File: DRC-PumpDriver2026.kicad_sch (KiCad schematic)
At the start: 28 parts, among them J1 STLINK, J10 VIN_PWR, J2 CAN, J3 CAN, J4 PUMP1, J5 PUMP2, J6 PUMP3, J7 PUMP4, J8 PUMP5, J9 PUMP6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

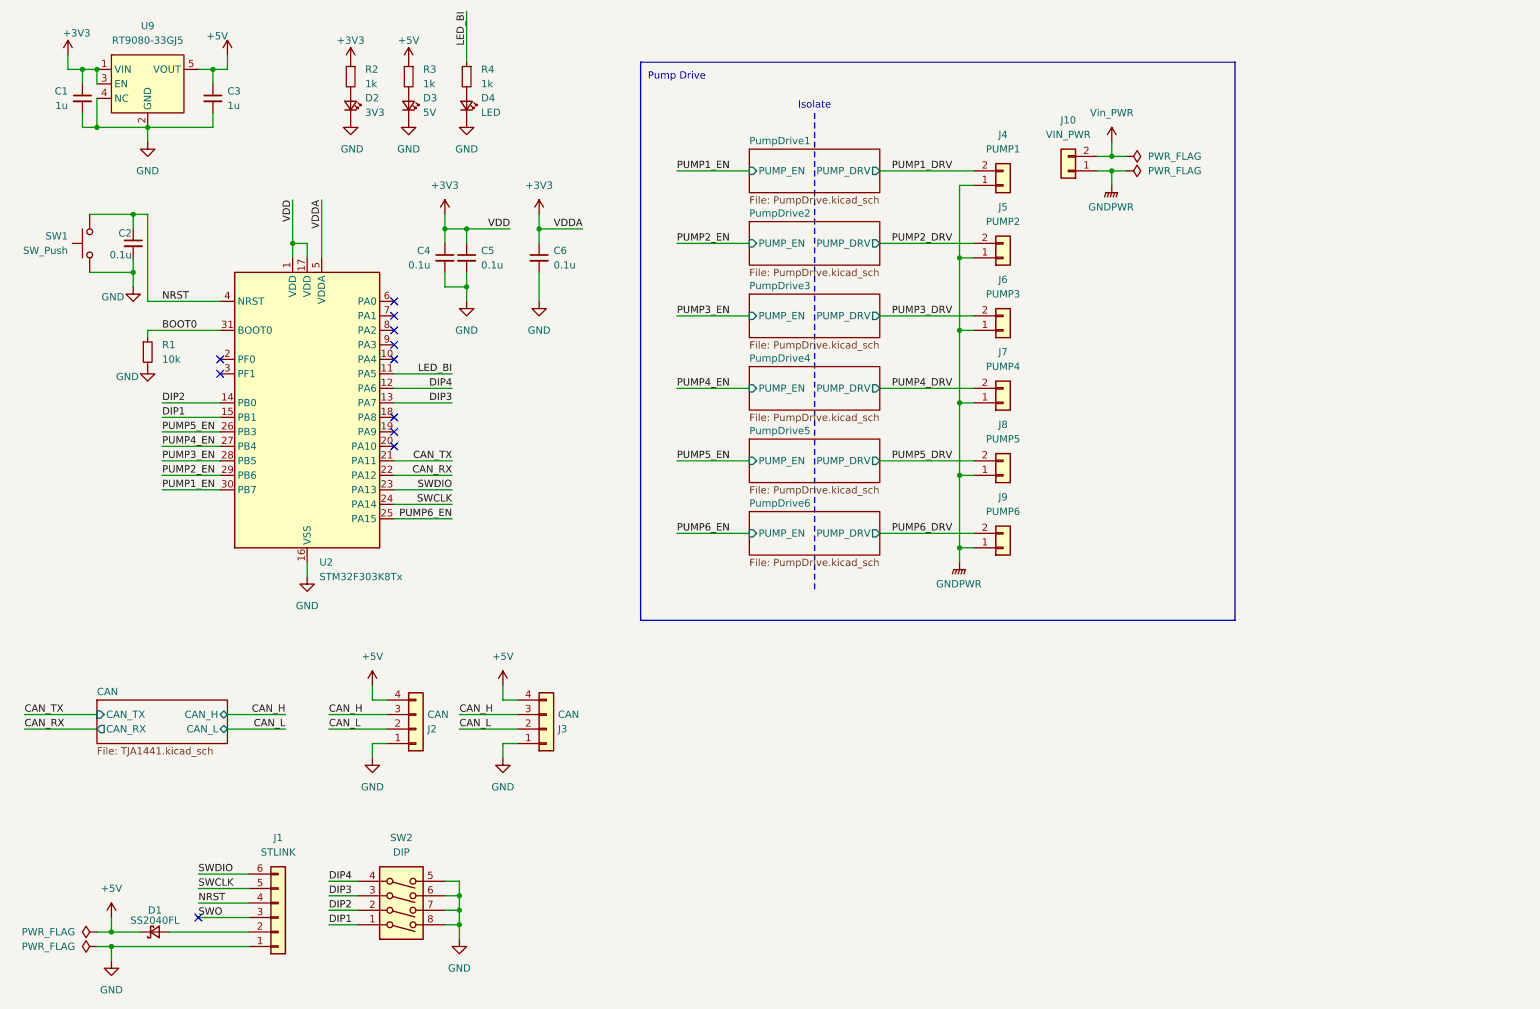
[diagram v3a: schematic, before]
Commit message: STLINK書込みをボックスヘッダへ、USB追加、v0.1.0
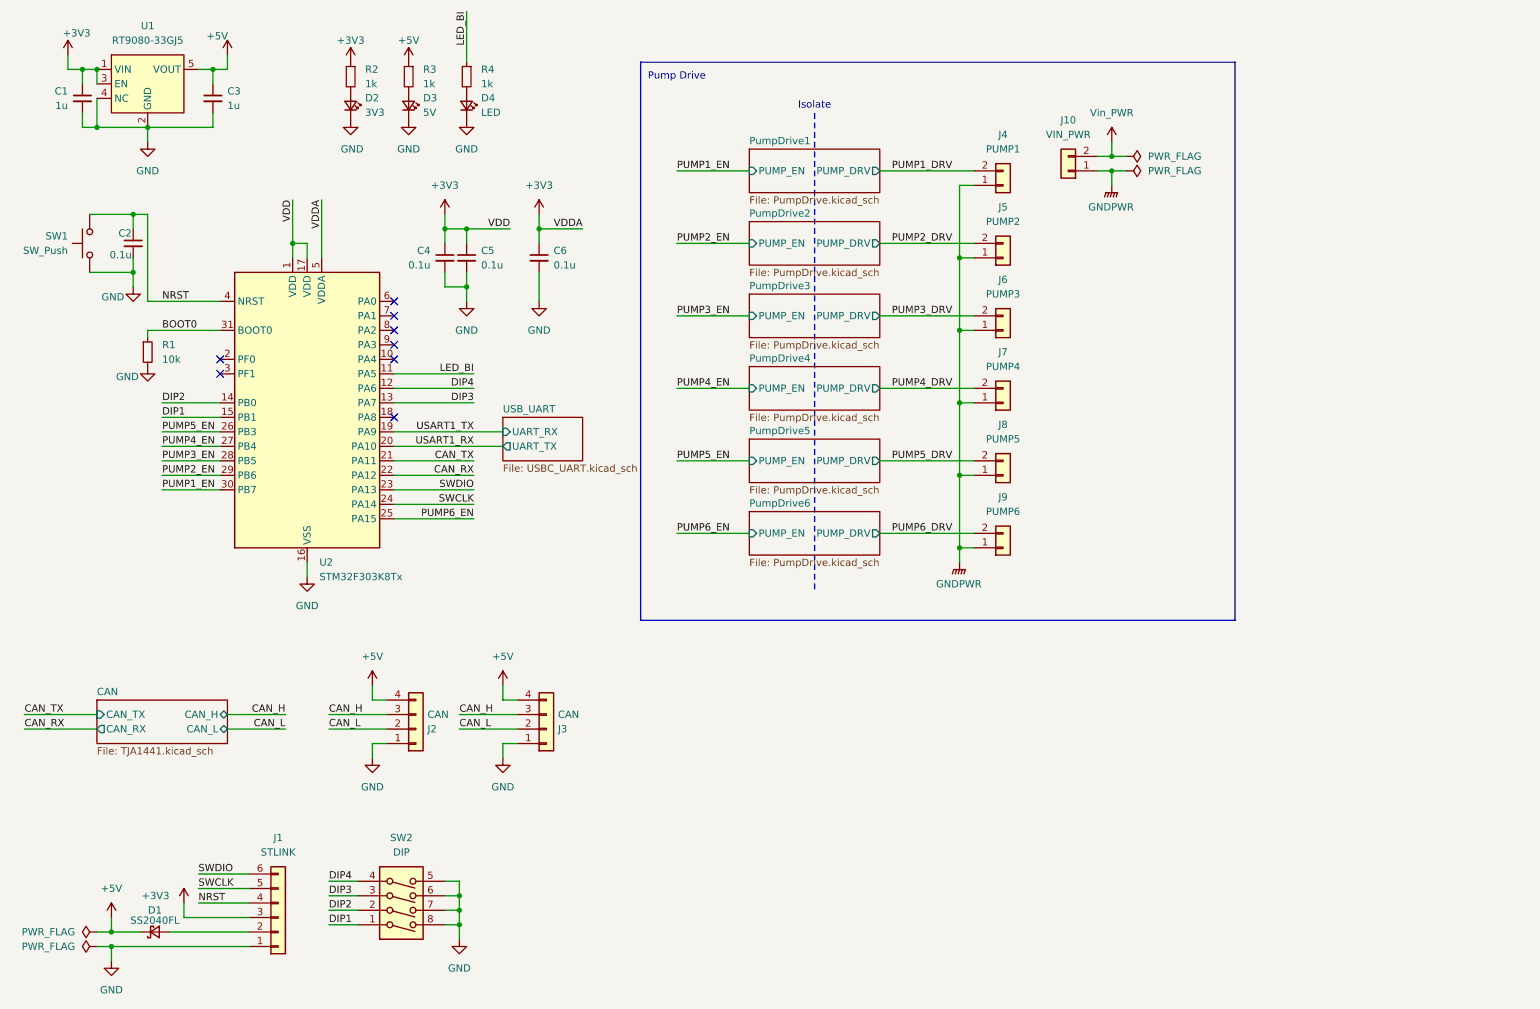
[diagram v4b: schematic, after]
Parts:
- J1: footprint Connector_JST:JST_PH_S6B-PH-K_1x06_P2.00mm_Horizontal -> Connector_IDC:IDC-Header_2x03_P2.54mm_Vertical
- renumbered U9 to U1
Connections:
- net SWO is gone; now on net +3V3: J1.3 (Pin_3)
- net USART1_TX: now reaches U2.19 (PA9)
- net USART1_RX: now reaches U2.20 (PA10)
- no-connect marks 11 -> 8
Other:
- added sheet USB_UART (USBC_UART.kicad_sch)
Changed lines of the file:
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@@
 	)
 	(no_connect
-		(at 85.09 87.63)
-	)
-	(no_connect
 		(at 85.09 67.31)
 	)
@@
 	)
 	(no_connect
-		(at 85.09 90.17)
-	)
-	(no_connect
-		(at 50.8 172.72)
-	)
-	(no_connect
 		(at 85.09 74.93)
 	)
@@
 	(wire
 		(pts
+			(xy 85.09 87.63) (xy 104.14 87.63)
+		)
+		(stroke
+			(width 0)
+			(type default)
+		)
+	)
+	(wire
+		(pts
 			(xy 41.91 64.77) (xy 54.61 64.77)
 		)
@@
 	(wire
 		(pts
+			(xy 48.26 170.18) (xy 48.26 172.72)
+		)
+		(stroke
+			(width 0)
+			(type default)
+		)
+	)
+	(wire
+		(pts
 			(xy 50.8 167.64) (xy 59.69 167.64)
 		)
@@
 	(wire
 		(pts
-			(xy 85.09 92.71) (xy 95.25 92.71)
+			(xy 85.09 92.71) (xy 99.06 92.71)
 		)
 		(stroke
@@
 	(wire
 		(pts
-			(xy 85.09 82.55) (xy 95.25 82.55)
+			(xy 85.09 82.55) (xy 99.06 82.55)
 		)
 		(stroke
@@
 	(wire
 		(pts
-			(xy 85.09 102.87) (xy 95.25 102.87)
+			(xy 85.09 102.87) (xy 99.06 102.87)
 		)
 		(stroke
@@
 	(wire
 		(pts
-			(xy 85.09 80.01) (xy 95.25 80.01)
+			(xy 85.09 80.01) (xy 99.06 80.01)
 		)
 		(stroke
@@
 	(wire
 		(pts
-			(xy 85.09 100.33) (xy 95.25 100.33)
+			(xy 85.09 100.33) (xy 99.06 100.33)
 		)
 		(stroke
@@
 	(wire
 		(pts
+			(xy 85.09 90.17) (xy 104.14 90.17)
+		)
+		(stroke
+			(width 0)
+			(type default)
+		)
+	)
+	(wire
+		(pts
 			(xy 72.39 46.99) (xy 72.39 57.15)
 		)
@@
 	(wire
 		(pts
+			(xy 48.26 172.72) (xy 59.69 172.72)
+		)
+		(stroke
+			(width 0)
+			(type default)
+		)
+	)
+	(wire
+		(pts
 			(xy 96.52 171.45) (xy 96.52 173.99)
 		)
@@
 	(wire
 		(pts
-			(xy 50.8 172.72) (xy 59.69 172.72)
-		)
-		(stroke
-			(width 0)
-			(type default)
-		)
-	)
-	(wire
-		(pts
 			(xy 30.48 31.75) (xy 30.48 34.29)
 		)
@@
 	(wire
 		(pts
-			(xy 85.09 97.79) (xy 95.25 97.79)
+			(xy 85.09 97.79) (xy 99.06 97.79)
 		)
 		(stroke
@@
 	(wire
 		(pts
-			(xy 85.09 95.25) (xy 95.25 95.25)
+			(xy 85.09 95.25) (xy 99.06 95.25)
 		)
 		(stroke
@@
 	(wire
 		(pts
-			(xy 85.09 77.47) (xy 95.25 77.47)
+			(xy 85.09 77.47) (xy 99.06 77.47)
 		)
 		(stroke
@@
 	)
 	(label "LED_BI"
-		(at 95.25 77.47 180)
+		(at 99.06 77.47 180)
 		(effects
 			(font
@@
 	)
 	(label "SWCLK"
-		(at 95.25 100.33 180)
+		(at 99.06 100.33 180)
 		(effects
 			(font
@@
 	)
 	(label "DIP3"
-		(at 95.25 82.55 180)
+		(at 99.06 82.55 180)
 		(effects
 			(font
@@
 	)
 	(label "PUMP6_EN"
-		(at 95.25 102.87 180)
+		(at 99.06 102.87 180)
 		(effects
 			(font
@@
 	)
 	(label "CAN_TX"
-		(at 95.25 92.71 180)
+		(at 99.06 92.71 180)
 		(effects
 			(font
@@
 		)
 	)
+	(label "USART1_TX"
+		(at 99.06 87.63 180)
+		(effects
+			(font
+				(size 1.27 1.27)
+			)
+			(justify right bottom)
+		)
+	)
 	(label "PUMP1_DRV"
 		(at 182.88 41.91 180)
@@
 	)
 	(label "SWDIO"
-		(at 95.25 97.79 180)
+		(at 99.06 97.79 180)
 		(effects
 			(font
@@
 		)
 	)
-	(label "CAN_L"
-		(at 66.04 139.7 180)
+	(label "USART1_RX"
+		(at 99.06 90.17 180)
 		(effects
 			(font
@@
 		)
 	)
-	(label "SWO"
-		(at 50.8 172.72 0)
+	(label "CAN_L"
+		(at 66.04 139.7 180)
 		(effects
 			(font
 				(size 1.27 1.27)
 			)
-			(justify left bottom)
+			(justify right bottom)
 		)
 	)
@@
 	)
 	(label "CAN_RX"
-		(at 95.25 95.25 180)
+		(at 99.06 95.25 180)
 		(effects
 			(font
@@
 	)
 	(label "DIP4"
-		(at 95.25 80.01 180)
+		(at 99.06 80.01 180)
 		(effects
 			(font
@@
 		(dnp no)
 		(fields_autoplaced yes)
-		(property "Reference" "#PWR02"
+		(property "Reference" "#PWR03"
 			(at 35.56 186.69 0)
 			(effects
@@
 			(project "DRC-PumpDriver2026"
 				(path "/cf42be67-fab3-494c-b2b5-38aff4068810"
-					(reference "#PWR02")
+					(reference "#PWR03")
 					(unit 1)
 				)
@@
 		(on_board yes)
 		(dnp no)
-		(property "Reference" "#PWR07"
+		(property "Reference" "#PWR01"
 			(at 27.94 25.4 0)
 			(effects
@@
 			(project "DRC-PumpDriver2026"
 				(path "/cf42be67-fab3-494c-b2b5-38aff4068810"
-					(reference "#PWR07")
+					(reference "#PWR01")
 					(unit 1)
 				)
@@
 			)
 		)
-		(property "Footprint" "Connector_JST:JST_PH_S6B-PH-K_1x06_P2.00mm_Horizontal"
+		(property "Footprint" "Connector_IDC:IDC-Header_2x03_P2.54mm_Vertical"
 			(at 64.77 172.72 0)
 			(effects
@@
 		(on_board yes)
 		(dnp no)
-		(property "Reference" "#PWR03"
+		(property "Reference" "#PWR07"
 			(at 55.88 25.4 0)
 			(effects
@@
 			(project "DRC-PumpDriver2026"
 				(path "/cf42be67-fab3-494c-b2b5-38aff4068810"
-					(reference "#PWR03")
+					(reference "#PWR07")
 					(unit 1)
 				)
@@
 		(on_board yes)
 		(dnp no)
-		(property "Reference" "#PWR05"
+		(property "Reference" "#PWR06"
 			(at 41.91 82.55 0)
 			(effects
@@
 			(project "DRC-PumpDriver2026"
 				(path "/cf42be67-fab3-494c-b2b5-38aff4068810"
-					(reference "#PWR05")
+					(reference "#PWR06")
 					(unit 1)
 				)
@@
 		(dnp no)
 		(fields_autoplaced yes)
-		(property "Reference" "#PWR01"
+		(property "Reference" "#PWR02"
 			(at 35.56 176.53 0)
 			(effects
@@
 			(project "DRC-PumpDriver2026"
 				(path "/cf42be67-fab3-494c-b2b5-38aff4068810"
-					(reference "#PWR01")
+					(reference "#PWR02")
 					(unit 1)
 				)
@@
 	)
 	(symbol
+		(lib_id "power:+3V3")
+		(at 48.26 170.18 0)
+		(unit 1)
+		(exclude_from_sim no)
+		(in_bom yes)
+		(on_board yes)
+		(dnp no)
+		(fields_autoplaced yes)
+		(property "Reference" "#PWR050"
+			(at 48.26 173.99 0)
+			(effects
+				(font
+					(size 1.27 1.27)
+				)
+				(hide yes)
+			)
+		)
+		(property "Value" "+3V3"
+			(at 45.72 168.9099 0)
+			(effects
+				(font
+					(size 1.27 1.27)
+				)
+				(justify right)
+			)
+		)
+		(property "Footprint" ""
+			(at 48.26 170.18 0)
+			(effects
+				(font
+					(size 1.27 1.27)
+				)
+				(hide yes)
+			)
+		)
+		(property "Datasheet" ""
+			(at 48.26 170.18 0)
+			(effects
+				(font
+					(size 1.27 1.27)
+				)
+				(hide yes)
+			)
+		)
+		(property "Description" "Power symbol creates a global label with name \"+3V3\""
+			(at 48.26 170.18 0)
+			(effects
+				(font
+					(size 1.27 1.27)
+				)
+				(hide yes)
+			)
+		)
+		(pin "1"
+		)
+		(instances
+			(project "DRC-PumpDriver2026"
+				(path "/cf42be67-fab3-494c-b2b5-38aff4068810"
+					(reference "#PWR050")
+					(unit 1)
+				)
+			)
+		)
+	)
+	(symbol
 		(lib_id "MCU_ST_STM32F3:STM32F303K8Tx")
 		(at 69.85 85.09 0)
@@
 		(dnp no)
 		(fields_autoplaced yes)
-		(property "Reference" "U9"
+		(property "Reference" "U1"
 			(at 41.91 16.51 0)
 			(effects
@@
 			(project "DRC-PumpDriver2026"
 				(path "/cf42be67-fab3-494c-b2b5-38aff4068810"
-					(reference "U9")
+					(reference "U1")
 					(unit 1)
 				)
@@
 		(dnp no)
 		(fields_autoplaced yes)
-		(property "Reference" "#PWR06"
+		(property "Reference" "#PWR05"
 			(at 41.91 43.18 0)
 			(effects
@@
 			(project "DRC-PumpDriver2026"
 				(path "/cf42be67-fab3-494c-b2b5-38aff4068810"
-					(reference "#PWR06")
+					(reference "#PWR05")
 					(unit 1)
 				)
@@
 				)
 			)
+		)
+	)
+	(sheet
+		(at 104.14 85.09)
+		(size 13.97 7.62)
+		(exclude_from_sim no)
+		(in_bom yes)
+		(on_board yes)
+		(dnp no)
+		(fields_autoplaced yes)
+		(stroke
+			(width 0.1524)
+			(type solid)
+		)
+		(fill
+			(color 0 0 0 0.0000)
+		)
+		(property "Sheetname" "USB_UART"
+			(at 104.14 84.3784 0)
+			(effects
+				(font
+					(size 1.27 1.27)
+				)
+				(justify left bottom)
+			)
+		)
+		(property "Sheetfile" "USBC_UART.kicad_sch"
+			(at 104.14 93.2946 0)
+			(effects
+				(font
+					(size 1.27 1.27)
+				)
+				(justify left top)
+			)
+		)
+		(pin "UART_RX" input
+			(at 104.14 87.63 180)
+			(effects
+				(font
+					(size 1.27 1.27)
+				)
+				(justify left)
+			)
+		)
+		(pin "UART_TX" output
+			(at 104.14 90.17 180)
+			(effects
+				(font
+					(size 1.27 1.27)
+				)
+				(justify left)
+			)
+		)
+		(instances
+			(project "DRC-PumpDriver2026"
+				(path "/cf42be67-fab3-494c-b2b5-38aff4068810"
+					(page "9")
+				)
+			)

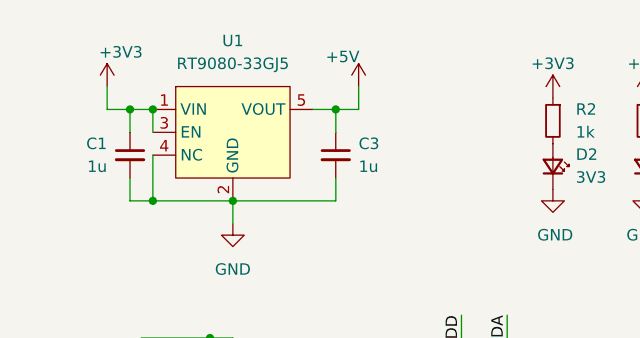
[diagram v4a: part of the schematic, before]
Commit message: レギュレータのフットプリントを修正
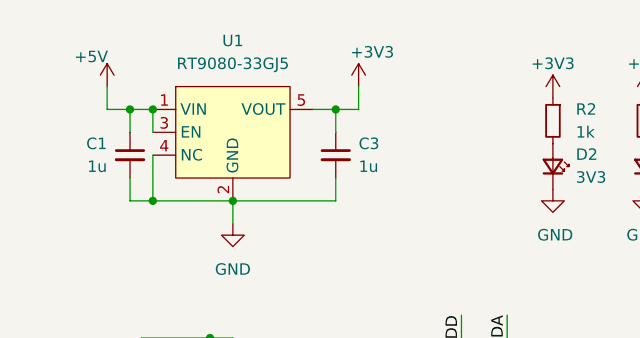
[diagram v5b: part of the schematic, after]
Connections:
- net +3V3: now also C3.1, U1.5 (VOUT); no longer C1.1, U1.1 (VIN), U1.3 (EN)
- net +5V: now also C1.1, U1.1 (VIN), U1.3 (EN); no longer C3.1, U1.5 (VOUT)
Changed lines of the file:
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@@
 	(symbol
 		(lib_id "power:+3V3")
-		(at 27.94 21.59 0)
+		(at 55.88 21.59 0)
 		(unit 1)
 		(exclude_from_sim no)
@@
 		(dnp no)
 		(property "Reference" "#PWR01"
-			(at 27.94 25.4 0)
+			(at 55.88 25.4 0)
 			(effects
 				(font
@@
 		)
 		(property "Value" "+3V3"
-			(at 29.464 17.78 0)
+			(at 57.404 17.78 0)
 			(effects
 				(font
@@
 		)
 		(property "Footprint" ""
-			(at 27.94 21.59 0)
+			(at 55.88 21.59 0)
 			(effects
 				(font
@@
 		)
 		(property "Datasheet" ""
-			(at 27.94 21.59 0)
+			(at 55.88 21.59 0)
 			(effects
 				(font
@@
 		)
 		(property "Description" "Power symbol creates a global label with name \"+3V3\""
-			(at 27.94 21.59 0)
+			(at 55.88 21.59 0)
 			(effects
 				(font
@@
 	(symbol
 		(lib_id "power:+5V")
-		(at 55.88 21.59 0)
+		(at 27.94 21.59 0)
 		(unit 1)
 		(exclude_from_sim no)
@@
 		(dnp no)
 		(property "Reference" "#PWR07"
-			(at 55.88 25.4 0)
+			(at 27.94 25.4 0)
 			(effects
 				(font
@@
 		)
 		(property "Value" "+5V"
-			(at 54.102 18.288 0)
+			(at 26.162 18.288 0)
 			(effects
 				(font
@@
 		)
 		(property "Footprint" ""
-			(at 55.88 21.59 0)
+			(at 27.94 21.59 0)
 			(effects
 				(font
@@
 		)
 		(property "Datasheet" ""
-			(at 55.88 21.59 0)
+			(at 27.94 21.59 0)
 			(effects
 				(font
@@
 		)
 		(property "Description" "Power symbol creates a global label with name \"+5V\""
-			(at 55.88 21.59 0)
-			(effects
-				(font
+			(at 27.94 21.59 0)
+			(effects
+				(font
